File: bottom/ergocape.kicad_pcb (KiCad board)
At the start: 2 copper layers, 183.2 x 140.8 mm, 9 parts

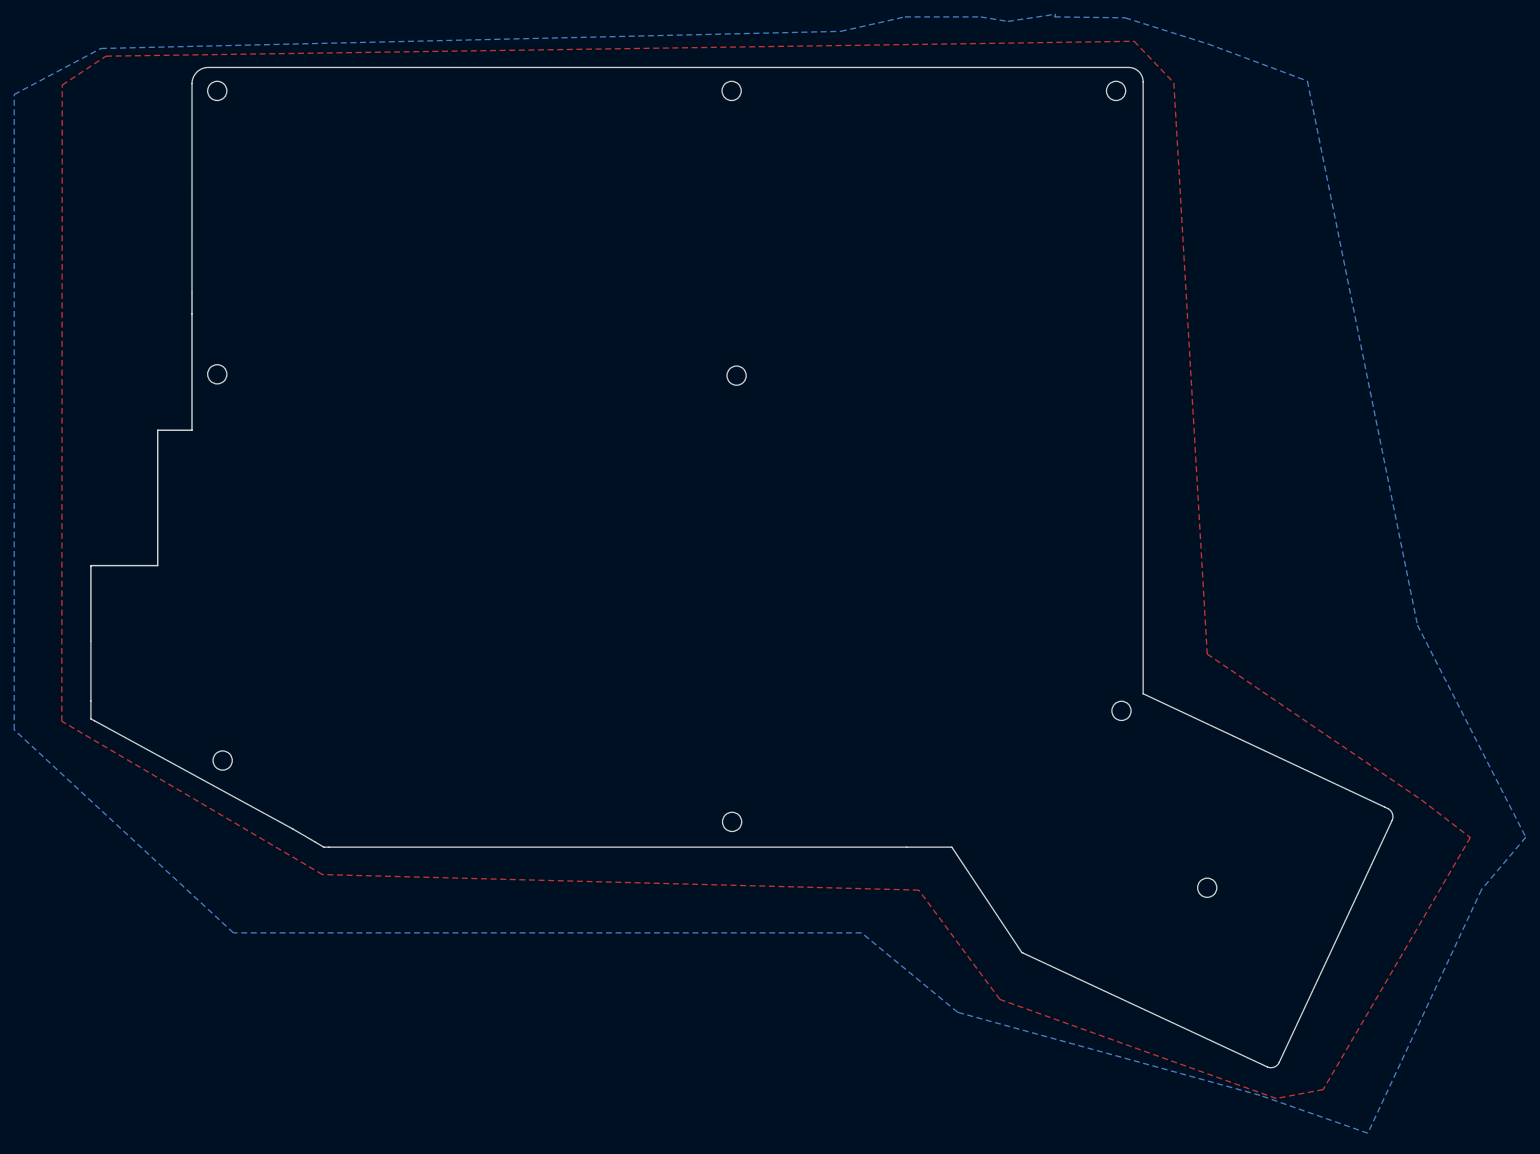
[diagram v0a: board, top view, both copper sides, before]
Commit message: fix pro micro footprint
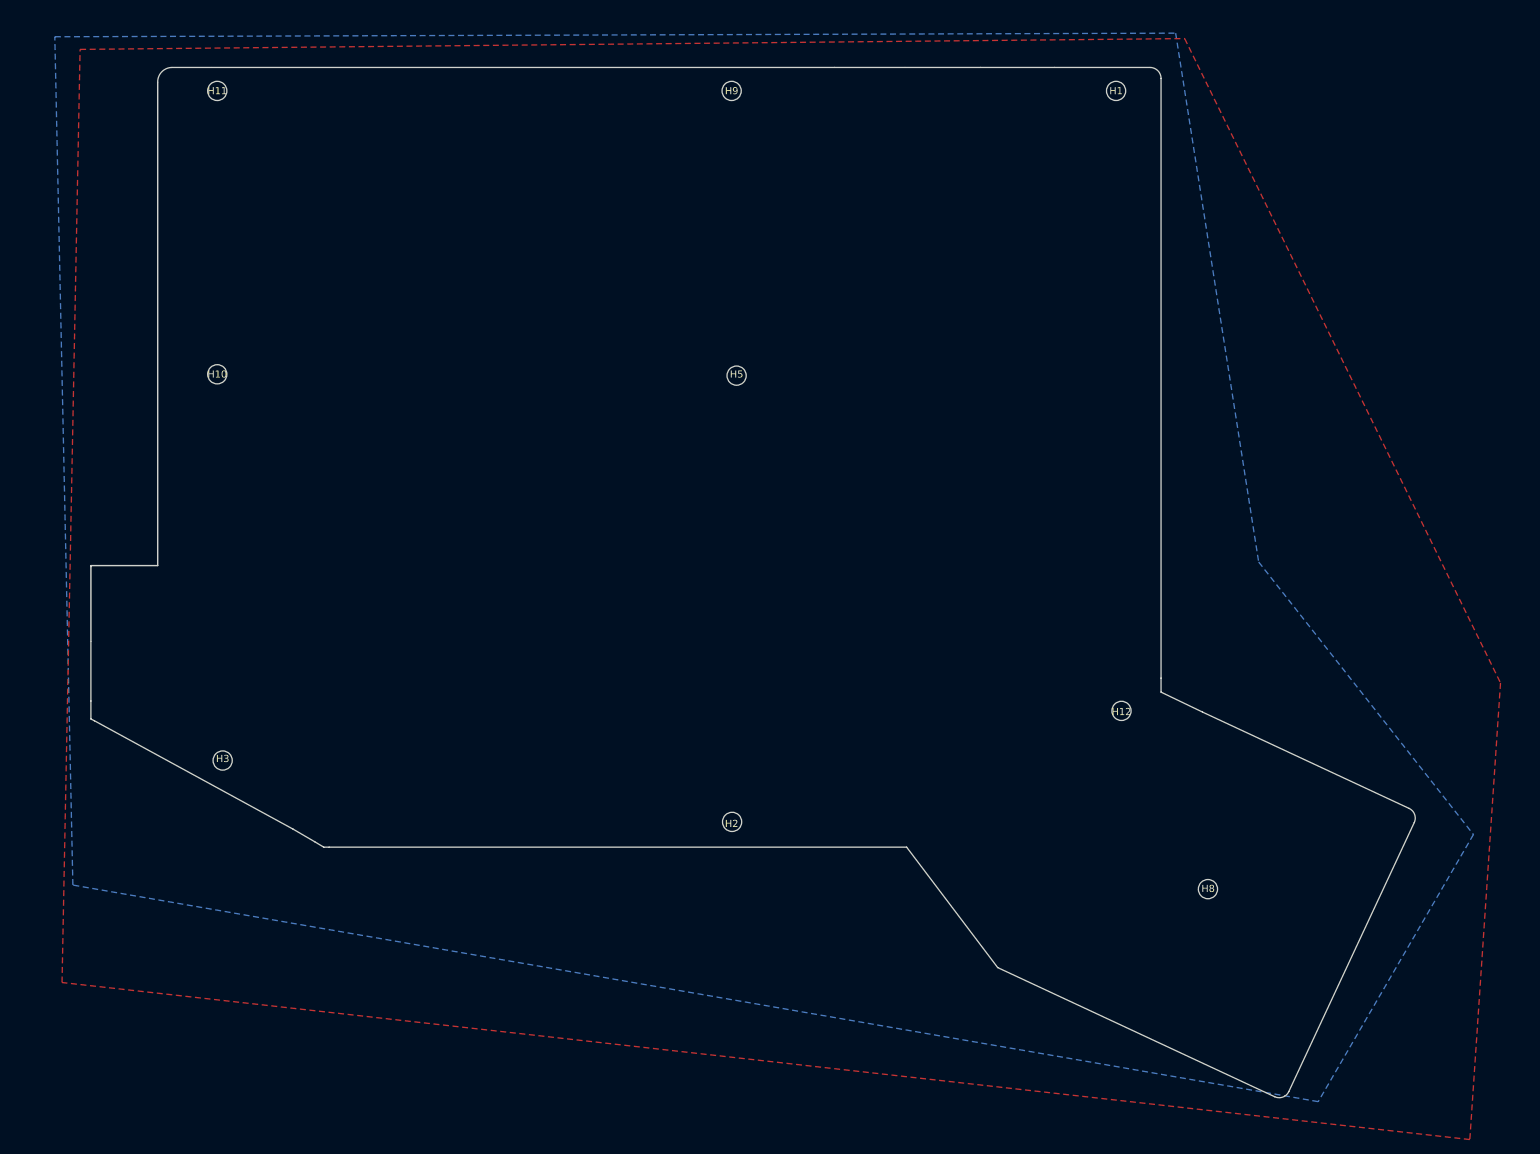
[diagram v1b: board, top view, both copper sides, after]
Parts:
- moved H8 0.22 mm to (179.6, 132.9)
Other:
- board size 183.2 x 140.8 mm -> 186.4 x 145 mm
